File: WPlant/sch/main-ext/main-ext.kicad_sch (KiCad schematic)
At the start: 69 parts, among them J1 PROG/JTAG, J10 Ext, J9 Leak, M1 Motor_DC, Q6 Si2301, Q7 BC817, SW1 SW_Push, SW2 SW_Push, SW3 SW_Push, U1 SIWG917Y121MGABAR, U10 SP485EEN-L/TR, U11 TXU0102QDCURQ1, U9 INA180A2, X1 SIT1552AI-JE-DCC-32.768D

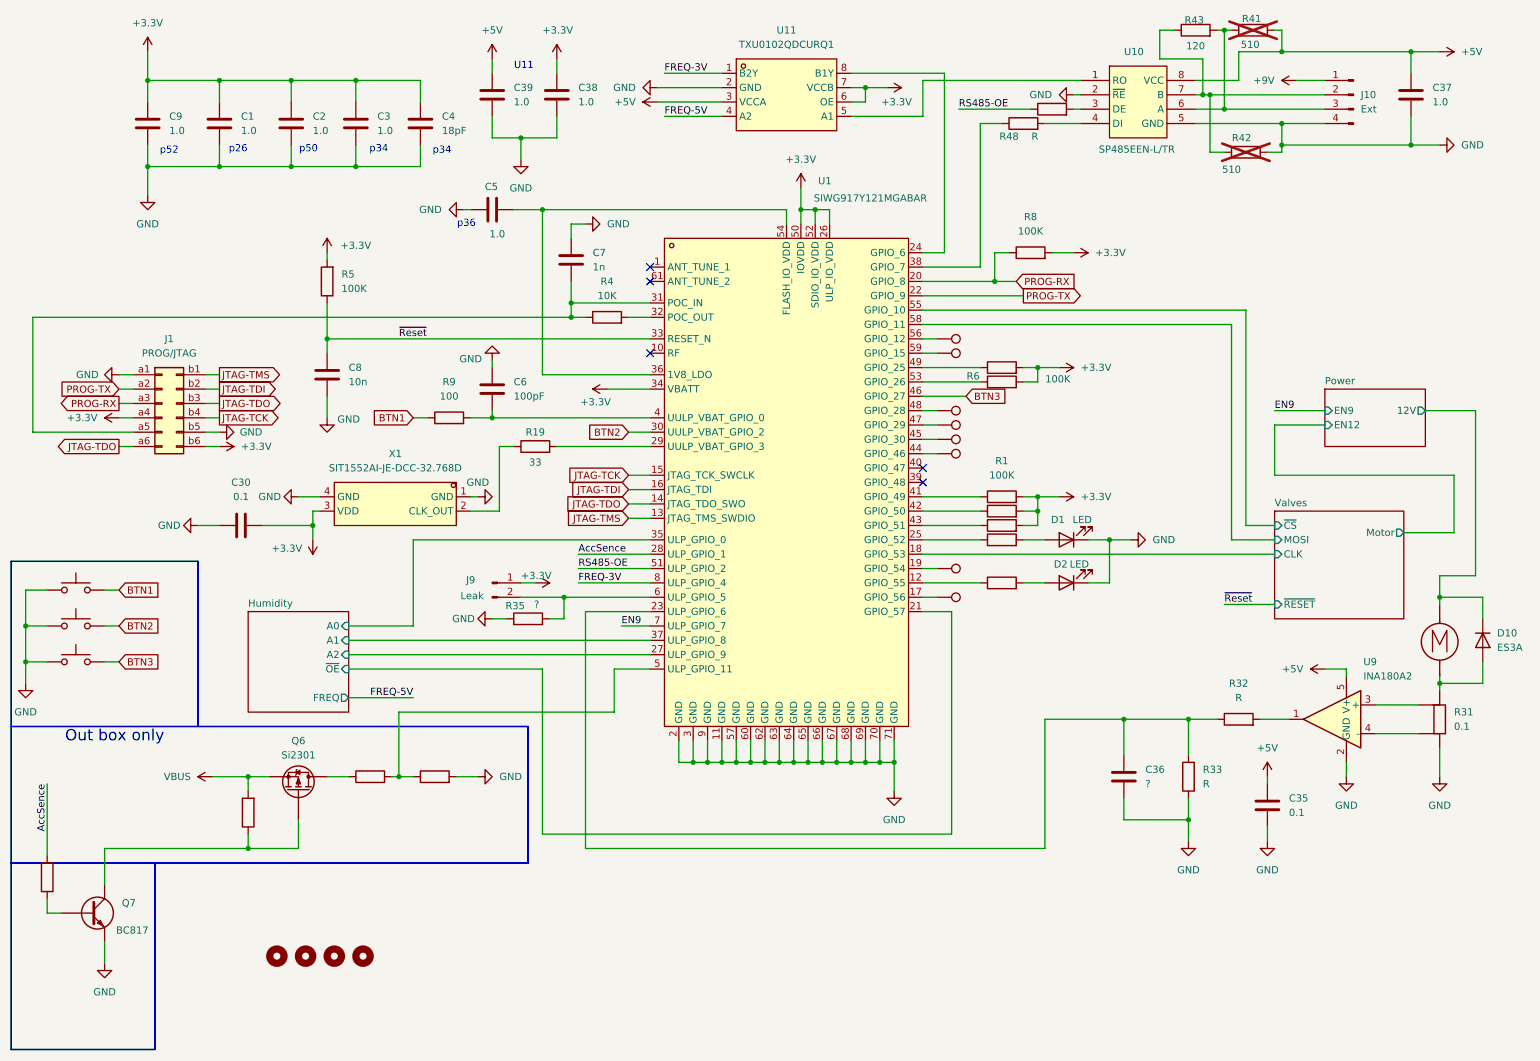
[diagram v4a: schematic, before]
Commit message: Upate values in SCH of WP
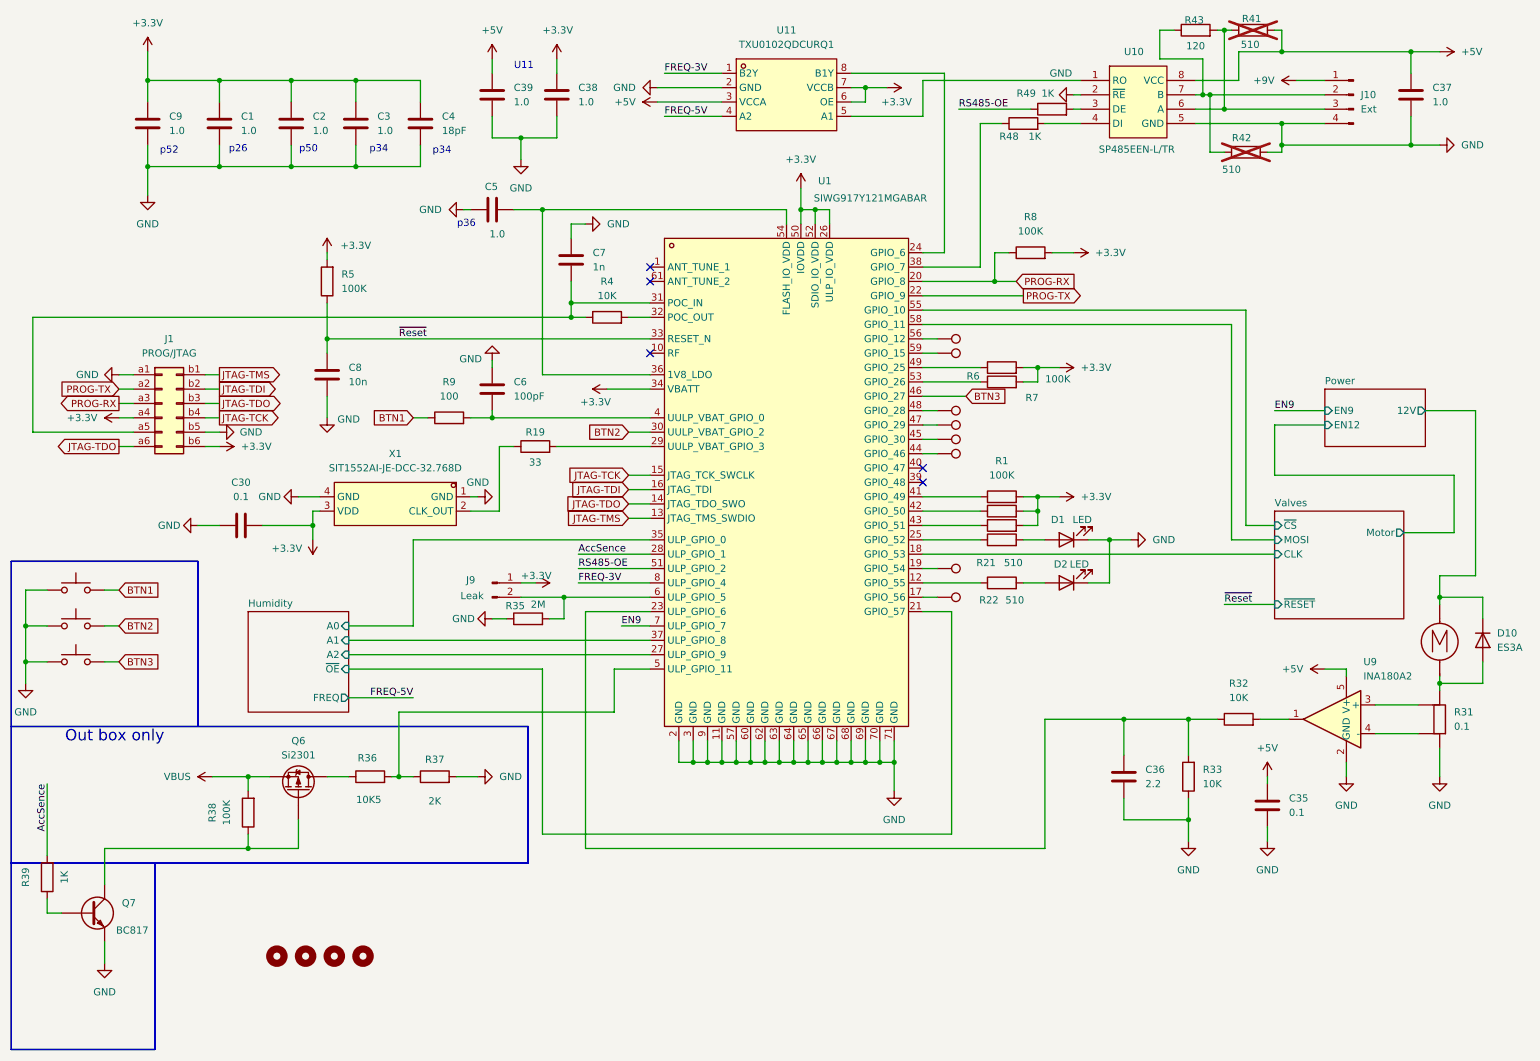
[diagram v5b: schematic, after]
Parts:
- C36: value ? -> 2.2
- R21, R22: value 100K -> 510
- R32, R33: value R -> 10K
- R35: value ? -> 2M
- R36: value 100K -> 10K5
- R37: value 100K -> 2K
- R39: value 100K -> 1K
- R48, R49: value R -> 1K
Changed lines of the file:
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@@
 		(on_board yes)
 		(dnp no)
-		(fields_autoplaced yes)
 		(property "Reference" "#PWR092"
 			(at 196.85 26.67 0)
@@
 		)
 		(property "Value" "GND"
-			(at 199.39 26.6699 90)
+			(at 202.946 22.86 90)
 			(effects
 				(font
@@
 		(dnp no)
 		(property "Reference" "R49"
-			(at 196.85 31.496 90)
+			(at 194.818 26.416 90)
 			(effects
 				(font
 					(size 1.27 1.27)
 				)
-				(hide yes)
 			)
 		)
-		(property "Value" "R"
-			(at 201.422 31.496 90)
+		(property "Value" "1K"
+			(at 198.628 26.416 90)
 			(effects
 				(font
 					(size 1.27 1.27)
 				)
-				(hide yes)
 			)
 		)
@@
 		(on_board yes)
 		(dnp no)
-		(fields_autoplaced yes)
 		(property "Reference" "R22"
-			(at 190.5 106.68 90)
+			(at 188.214 116.078 90)
 			(effects
 				(font
 					(size 1.27 1.27)
 				)
-				(hide yes)
 			)
 		)
-		(property "Value" "100K"
-			(at 190.5 109.22 90)
+		(property "Value" "510"
+			(at 192.786 116.078 90)
 			(effects
 				(font
 					(size 1.27 1.27)
 				)
-				(hide yes)
 			)
 		)
@@
 		(on_board yes)
 		(dnp no)
-		(fields_autoplaced yes)
 		(property "Reference" "R39"
-			(at 15.24 165.1 90)
+			(at 17.78 165.1 90)
 			(effects
 				(font
 					(size 1.27 1.27)
 				)
-				(hide yes)
 			)
 		)
-		(property "Value" "100K"
-			(at 17.78 165.1 90)
+		(property "Value" "1K"
+			(at 24.638 165.1 90)
 			(effects
 				(font
 					(size 1.27 1.27)
 				)
-				(hide yes)
 			)
 		)
@@
 			)
 		)
-		(property "Value" "R"
+		(property "Value" "10K"
 			(at 226.06 148.5899 0)
 			(effects
@@
 		(on_board yes)
 		(dnp no)
-		(fields_autoplaced yes)
 		(property "Reference" "R21"
-			(at 190.5 99.06 90)
+			(at 187.706 109.474 90)
 			(effects
 				(font
 					(size 1.27 1.27)
 				)
-				(hide yes)
 			)
 		)
-		(property "Value" "100K"
-			(at 190.5 101.6 90)
+		(property "Value" "510"
+			(at 192.532 109.474 90)
 			(effects
 				(font
 					(size 1.27 1.27)
 				)
-				(hide yes)
 			)
 		)
@@
 		(on_board yes)
 		(dnp no)
-		(fields_autoplaced yes)
 		(property "Reference" "R36"
-			(at 78.74 140.97 90)
+			(at 78.232 144.018 90)
 			(effects
 				(font
 					(size 1.27 1.27)
 				)
-				(hide yes)
 			)
 		)
-		(property "Value" "100K"
-			(at 78.74 143.51 90)
+		(property "Value" "10K5"
+			(at 78.486 151.384 90)
 			(effects
 				(font
 					(size 1.27 1.27)
 				)
-				(hide yes)
 			)
 		)
@@
 					(size 1.27 1.27)
 				)
-				(hide yes)
 			)
 		)
@@
 					(size 1.27 1.27)
 				)
-				(hide yes)
 			)
 		)
@@
 		(on_board yes)
 		(dnp no)
-		(fields_autoplaced yes)
 		(property "Reference" "R37"
-			(at 90.17 140.97 90)
+			(at 90.17 144.272 90)
 			(effects
 				(font
 					(size 1.27 1.27)
 				)
-				(hide yes)
 			)
 		)
-		(property "Value" "100K"
-			(at 90.17 143.51 90)
+		(property "Value" "2K"
+			(at 90.17 151.638 90)
 			(effects
 				(font
 					(size 1.27 1.27)
 				)
-				(hide yes)
 			)
 		)
@@
 			)
 		)
-		(property "Value" "R"
+		(property "Value" "1K"
 			(at 196.342 34.036 90)
 			(effects
@@
 			)
 		)
-		(property "Value" "?"
-			(at 108.204 116.84 90)
+		(property "Value" "2M"
+			(at 108.458 116.84 90)
 			(effects
 				(font
@@
 			)
 		)
-		(property "Value" "R"
+		(property "Value" "10K"
 			(at 232.41 133.35 90)
 			(effects
@@
 			)
 		)
-		(property "Value" "?"
+		(property "Value" "2.2"
 			(at 215.9 148.5899 0)
 			(effects
@@
 		(on_board yes)
 		(dnp no)
-		(fields_autoplaced yes)
 		(property "Reference" "R7"
-			(at 190.5 71.12 90)
+			(at 195.834 80.264 90)
 			(effects
 				(font
 					(size 1.27 1.27)
 				)
-				(hide yes)
 			)
 		)

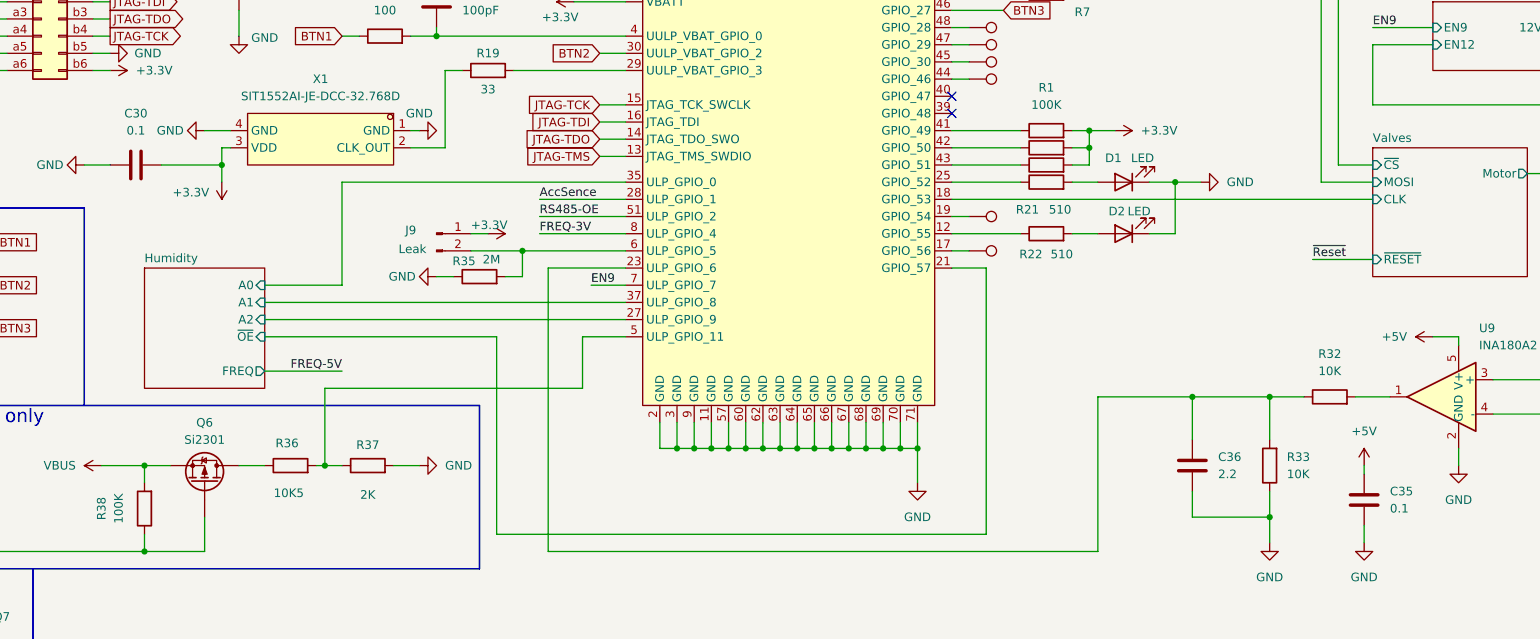
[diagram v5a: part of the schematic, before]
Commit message: Update WP Sch (sheets titles, replaced wires by bus, update components values)
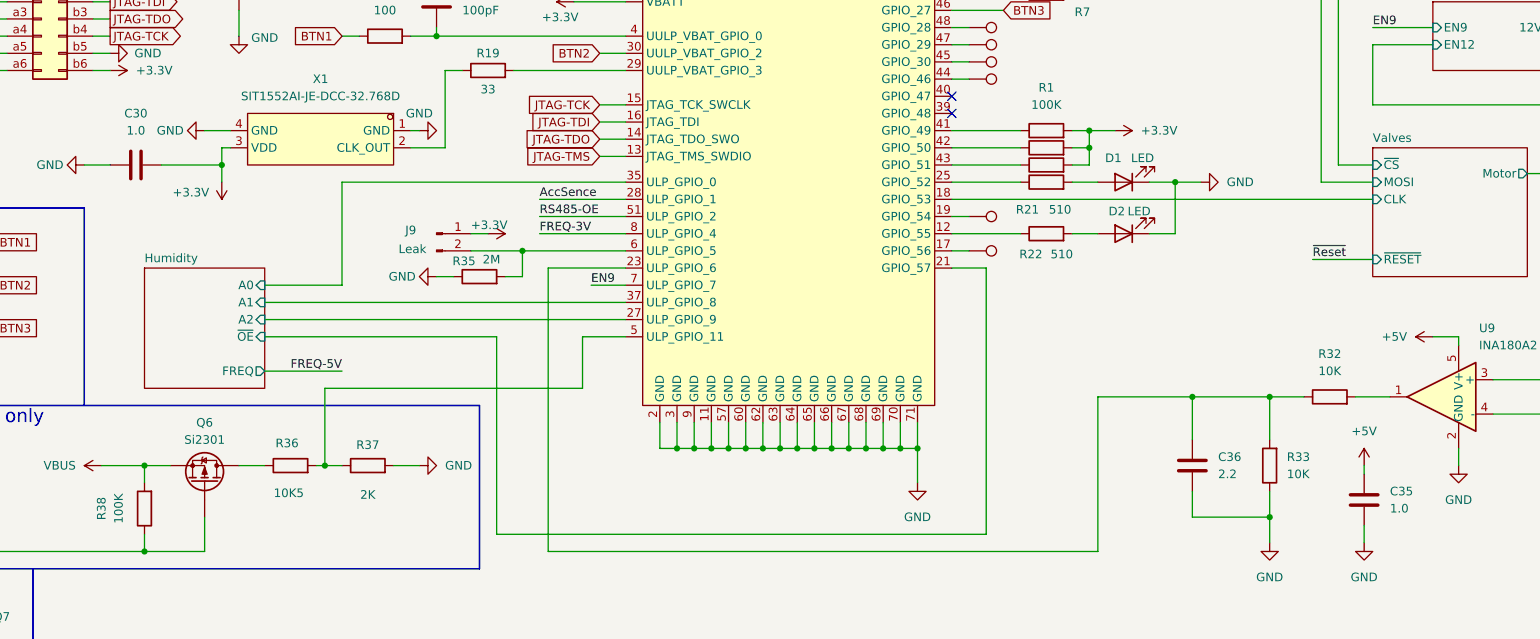
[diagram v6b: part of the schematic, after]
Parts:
- C30, C35: value 0.1 -> 1.0
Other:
- title: Water Plant main module -> Water Plant main module (External)
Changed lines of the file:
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@@
 	(paper "A4")
 	(title_block
-		(title "Water Plant main module")
+		(title "Water Plant main module (External)")
+		(date "2026-02-05")
 		(company "RoboWay")
 	)
@@
 			)
 		)
-		(property "Value" "0.1"
+		(property "Value" "1.0"
 			(at 55.88 97.79 90)
 			(effects
@@
 			)
 		)
-		(property "Value" "0.1"
+		(property "Value" "1.0"
 			(at 241.3 153.6699 0)
 			(effects
